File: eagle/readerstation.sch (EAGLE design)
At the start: 15 parts, among them IC1 PCF8574P, IC2 SPX1117

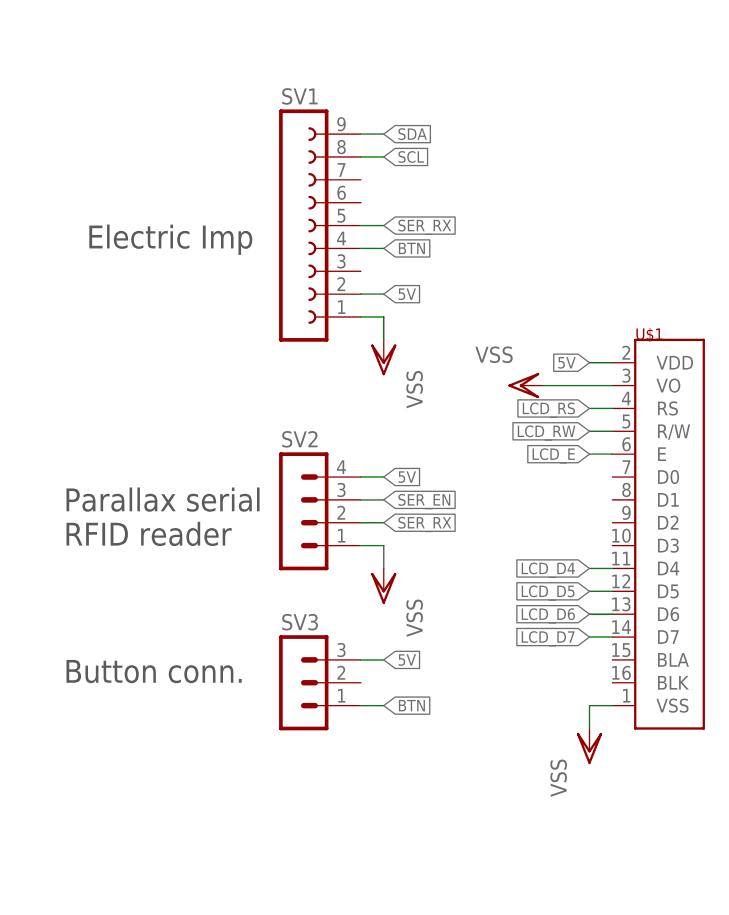
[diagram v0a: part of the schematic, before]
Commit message: Added series resistors in a couple of places on the readerstation that I originally missed
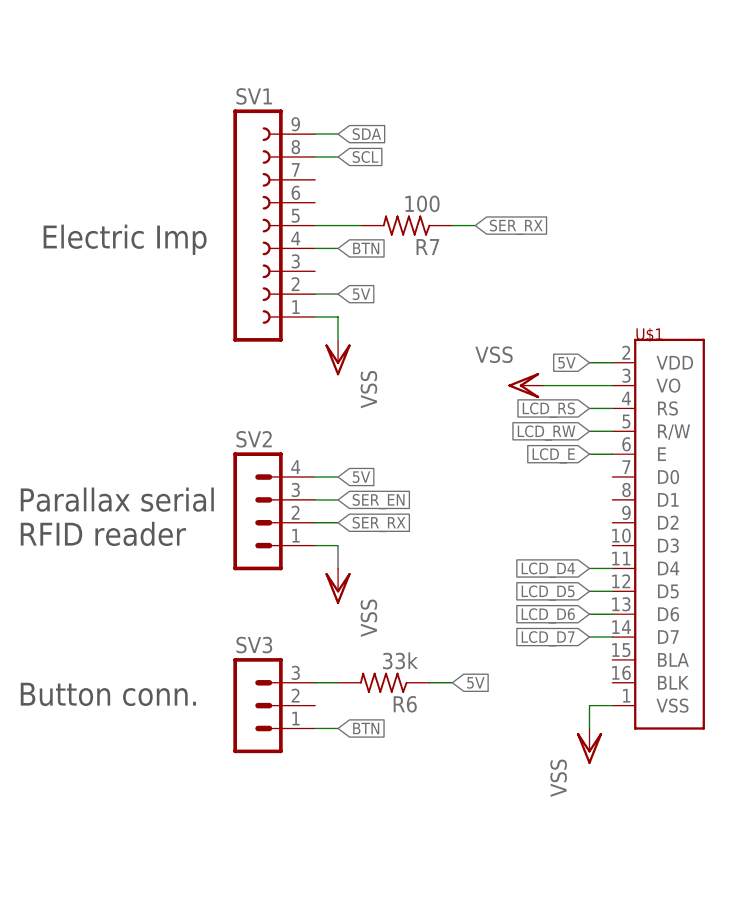
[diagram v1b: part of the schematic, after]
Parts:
- added R6: 33k, rcl:R-US_0204/5
- added R7: 100, rcl:R-US_0204/5
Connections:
- new net N$10: R6.2, SV3.3
- new net N$2: R7.2, SV1.5
- net 5V: now also R6.1; no longer SV3.3
- net SER_RX: now also R7.1; no longer SV1.5
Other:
- moved on the sheet: SV1, SV2, SV3
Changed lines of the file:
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@@
 <setting verticaltext="up"/>
 </settings>
-<grid distance="0.1" unitdist="inch" unit="inch" style="lines" multiple="1" display="yes" altdistance="0.01" altunitdist="inch" altunit="inch"/>
+<grid distance="0.1" unitdist="inch" unit="inch" style="lines" multiple="1" display="no" altdistance="0.01" altunitdist="inch" altunit="inch"/>
 <layers>
 <layer number="1" name="Top" color="4" fill="1" visible="no" active="no"/>
@@
 <part name="VSS11" library="supply1" deviceset="VSS" device=""/>
 <part name="FRAME1" library="frames" deviceset="A4L-LOC" device=""/>
+<part name="R6" library="rcl" deviceset="R-US_" device="0204/5" value="33k"/>
+<part name="R7" library="rcl" deviceset="R-US_" device="0204/5" value="100"/>
 </parts>
 <sheets>
 <sheet>
 <plain>
-<text x="-38.1" y="53.34" size="2.54" layer="97">Electric Imp</text>
-<text x="-40.64" y="20.32" size="2.54" layer="97">Parallax serial
+<text x="-43.18" y="53.34" size="2.54" layer="97">Electric Imp</text>
+<text x="-45.72" y="20.32" size="2.54" layer="97">Parallax serial
 RFID reader</text>
-<wire x1="-5.08" y1="20.32" x2="-5.08" y2="17.78" width="0.1524" layer="97"/>
-<text x="-40.64" y="5.08" size="2.54" layer="97">Button conn.</text>
+<wire x1="-10.16" y1="20.32" x2="-10.16" y2="17.78" width="0.1524" layer="97"/>
+<text x="-45.72" y="2.54" size="2.54" layer="97">Button conn.</text>
 <text x="132.08" y="-43.18" size="2.54" layer="94" font="vector">KBEmbedded 2015</text>
 </plain>
 <instances>
 <instance part="U$1" gate="G$1" x="30.48" y="27.94"/>
-<instance part="SV1" gate="G$1" x="-15.24" y="55.88"/>
+<instance part="SV1" gate="G$1" x="-20.32" y="55.88"/>
 <instance part="G1" gate="G$1" x="58.42" y="63.5" rot="R90"/>
 <instance part="IC1" gate="G$1" x="83.82" y="12.7"/>
@@
 <instance part="R3" gate="G$1" x="66.04" y="27.94" rot="R90"/>
 <instance part="VSS5" gate="G$1" x="116.84" y="12.7" rot="MR0"/>
-<instance part="VSS6" gate="G$1" x="-5.08" y="40.64" rot="MR0"/>
-<instance part="SV2" gate="1" x="-15.24" y="25.4"/>
-<instance part="SV3" gate="G$1" x="-15.24" y="5.08"/>
-<instance part="VSS7" gate="G$1" x="-5.08" y="15.24" rot="MR0"/>
+<instance part="VSS6" gate="G$1" x="-10.16" y="40.64" rot="MR0"/>
+<instance part="SV2" gate="1" x="-20.32" y="25.4"/>
+<instance part="SV3" gate="G$1" x="-20.32" y="2.54"/>
+<instance part="VSS7" gate="G$1" x="-10.16" y="15.24" rot="MR0"/>
 <instance part="IC2" gate="G$1" x="78.74" y="76.2"/>
 <instance part="VSS8" gate="G$1" x="58.42" y="45.72" rot="MR0"/>
@@
 <instance part="VSS11" gate="G$1" x="93.98" y="66.04" rot="MR0"/>
 <instance part="FRAME1" gate="G$1" x="-86.36" y="-63.5"/>
+<instance part="R6" gate="G$1" x="-5.08" y="5.08" rot="R180"/>
+<instance part="R7" gate="G$1" x="-2.54" y="55.88" rot="R180"/>
 </instances>
 <busses>
@@
 <segment>
 <pinref part="SV1" gate="G$1" pin="4"/>
-<wire x1="-7.62" y1="53.34" x2="-5.08" y2="53.34" width="0.1524" layer="91"/>
-<label x="-5.08" y="53.34" size="1.27" layer="95" xref="yes"/>
+<wire x1="-12.7" y1="53.34" x2="-10.16" y2="53.34" width="0.1524" layer="91"/>
+<label x="-10.16" y="53.34" size="1.27" layer="95" xref="yes"/>
 </segment>
 <segment>
 <pinref part="SV3" gate="G$1" pin="1"/>
-<wire x1="-7.62" y1="2.54" x2="-5.08" y2="2.54" width="0.1524" layer="91"/>
-<label x="-5.08" y="2.54" size="1.27" layer="95" xref="yes"/>
+<wire x1="-12.7" y1="0" x2="-10.16" y2="0" width="0.1524" layer="91"/>
+<label x="-10.16" y="0" size="1.27" layer="95" xref="yes"/>
 </segment>
 </net>
 <net name="SER_RX" class="0">
 <segment>
-<pinref part="SV1" gate="G$1" pin="5"/>
-<wire x1="-7.62" y1="55.88" x2="-5.08" y2="55.88" width="0.1524" layer="91"/>
-<label x="-5.08" y="55.88" size="1.27" layer="95" xref="yes"/>
-</segment>
-<segment>
 <pinref part="SV2" gate="1" pin="2"/>
-<wire x1="-5.08" y1="22.86" x2="-7.62" y2="22.86" width="0.1524" layer="91"/>
-<label x="-5.08" y="22.86" size="1.27" layer="95" xref="yes"/>
+<wire x1="-10.16" y1="22.86" x2="-12.7" y2="22.86" width="0.1524" layer="91"/>
+<label x="-10.16" y="22.86" size="1.27" layer="95" xref="yes"/>
+</segment>
+<segment>
+<pinref part="R7" gate="G$1" pin="1"/>
+<wire x1="2.54" y1="55.88" x2="5.08" y2="55.88" width="0.1524" layer="91"/>
+<label x="5.08" y="55.88" size="1.27" layer="95" xref="yes"/>
 </segment>
 </net>
@@
 <segment>
 <pinref part="SV1" gate="G$1" pin="2"/>
-<wire x1="-7.62" y1="48.26" x2="-5.08" y2="48.26" width="0.1524" layer="91"/>
-<label x="-5.08" y="48.26" size="1.27" layer="95" xref="yes"/>
-</segment>
-<segment>
-<pinref part="SV3" gate="G$1" pin="3"/>
-<wire x1="-7.62" y1="7.62" x2="-5.08" y2="7.62" width="0.1524" layer="91"/>
-<label x="-5.08" y="7.62" size="1.27" layer="95" xref="yes"/>
+<wire x1="-12.7" y1="48.26" x2="-10.16" y2="48.26" width="0.1524" layer="91"/>
+<label x="-10.16" y="48.26" size="1.27" layer="95" xref="yes"/>
 </segment>
 <segment>
 <pinref part="SV2" gate="1" pin="4"/>
-<wire x1="-7.62" y1="27.94" x2="-5.08" y2="27.94" width="0.1524" layer="91"/>
-<label x="-5.08" y="27.94" size="1.27" layer="95" xref="yes"/>
+<wire x1="-12.7" y1="27.94" x2="-10.16" y2="27.94" width="0.1524" layer="91"/>
+<label x="-10.16" y="27.94" size="1.27" layer="95" xref="yes"/>
 </segment>
 <segment>
@@
 <wire x1="93.98" y1="76.2" x2="101.6" y2="76.2" width="0.1524" layer="91"/>
 <label x="101.6" y="76.2" size="1.27" layer="95" xref="yes"/>
+</segment>
+<segment>
+<pinref part="R6" gate="G$1" pin="1"/>
+<wire x1="0" y1="5.08" x2="2.54" y2="5.08" width="0.1524" layer="91"/>
+<label x="2.54" y="5.08" size="1.27" layer="95" xref="yes"/>
 </segment>
 </net>
@@
 <segment>
 <pinref part="SV1" gate="G$1" pin="1"/>
-<wire x1="-7.62" y1="45.72" x2="-5.08" y2="45.72" width="0.1524" layer="91"/>
+<wire x1="-12.7" y1="45.72" x2="-10.16" y2="45.72" width="0.1524" layer="91"/>
 <pinref part="VSS6" gate="G$1" pin="VSS"/>
-<wire x1="-5.08" y1="45.72" x2="-5.08" y2="43.18" width="0.1524" layer="91"/>
+<wire x1="-10.16" y1="45.72" x2="-10.16" y2="43.18" width="0.1524" layer="91"/>
 </segment>
 <segment>
@@
 <segment>
 <pinref part="SV2" gate="1" pin="3"/>
-<wire x1="-7.62" y1="25.4" x2="-5.08" y2="25.4" width="0.1524" layer="91"/>
-<label x="-5.08" y="25.4" size="1.27" layer="95" xref="yes"/>
+<wire x1="-12.7" y1="25.4" x2="-10.16" y2="25.4" width="0.1524" layer="91"/>
+<label x="-10.16" y="25.4" size="1.27" layer="95" xref="yes"/>
 </segment>
 </net>
@@
 <segment>
 <pinref part="SV1" gate="G$1" pin="8"/>
-<wire x1="-7.62" y1="63.5" x2="-5.08" y2="63.5" width="0.1524" layer="91"/>
-<label x="-5.08" y="63.5" size="1.27" layer="95" xref="yes"/>
+<wire x1="-12.7" y1="63.5" x2="-10.16" y2="63.5" width="0.1524" layer="91"/>
+<label x="-10.16" y="63.5" size="1.27" layer="95" xref="yes"/>
 </segment>
 </net>
@@
 <segment>
 <pinref part="SV1" gate="G$1" pin="9"/>
-<wire x1="-7.62" y1="66.04" x2="-5.08" y2="66.04" width="0.1524" layer="91"/>
-<label x="-5.08" y="66.04" size="1.27" layer="95" xref="yes"/>
+<wire x1="-12.7" y1="66.04" x2="-10.16" y2="66.04" width="0.1524" layer="91"/>
+<label x="-10.16" y="66.04" size="1.27" layer="95" xref="yes"/>
 </segment>
 </net>
@@
 <segment>
 <pinref part="SV2" gate="1" pin="1"/>
-<wire x1="-7.62" y1="20.32" x2="-5.08" y2="20.32" width="0.1524" layer="91"/>
+<wire x1="-12.7" y1="20.32" x2="-10.16" y2="20.32" width="0.1524" layer="91"/>
 </segment>
 </net>
@@
 </segment>
 </net>
+<net name="N$10" class="0">
+<segment>
+<pinref part="SV3" gate="G$1" pin="3"/>
+<wire x1="-12.7" y1="5.08" x2="-10.16" y2="5.08" width="0.1524" layer="91"/>
+<pinref part="R6" gate="G$1" pin="2"/>
+</segment>
+</net>
+<net name="N$2" class="0">
+<segment>
+<pinref part="SV1" gate="G$1" pin="5"/>
+<wire x1="-12.7" y1="55.88" x2="-10.16" y2="55.88" width="0.1524" layer="91"/>
+<pinref part="R7" gate="G$1" pin="2"/>
+<wire x1="-10.16" y1="55.88" x2="-7.62" y2="55.88" width="0.1524" layer="91"/>
+</segment>
+</net>
